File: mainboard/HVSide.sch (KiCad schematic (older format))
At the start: 36 parts, among them J10 IMD_TS-, J7 ProminentIndicator, J8 HV, J9 IMD_TS+, Q15 BULB49D, Q16 TSM2312, U13 ISOW7841, U14 LTC1865L, U15 LTC6259, U16 REF3433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

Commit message: change isoadc in schematic and documents
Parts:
- removed unit 2 of U13
- removed U14: LTC1865L, Package_SO:SSOP-10_3.9x4.9mm_P1.00mm, symbol MainBoard:LTC1865L
- added C13: 10n, symbol Device:C_Small
- added R52, R53: 22, symbol Device:R
- added R54: 2k, symbol Device:R_Small
- added R55: 680, symbol Device:R_Small
- added R56: 100k, symbol Device:R_Small
- added U14: Si8900, symbol si8900:Si8900
- added U20: TCMT1103, Package_SO:SOP-4_4.4x2.6mm_P1.27mm, symbol Isolator:TCMT1103
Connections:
- net labels added: ISOADC_RX, ISOADC_TX, RST_ADCB, ~RST~_ADCA
- net labels removed: CS, MISO, MOSI, SCK
- wire segments 135 -> 146
- no-connect marks 0 -> 6
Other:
- note removed: "UPDATE COMPONENT TO 10 PIN PACKAGE"

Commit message: i2c isoadc 8901
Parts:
- removed U14: Si8900, symbol si8900:Si8900
- added R?: 5k, symbol Device:R
- added U?: Si8901, symbol si8900:Si8901
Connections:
- net +3V3: now also U?.10 (VDDB), U?.16 (VDDB)
- net -BATT: now also U?.8 (GNDA)
- net 3V3ISO: now also R?.2, U?.1 (VDDA)
- net GND: now also U?.9 (GNDB)
- net PackV: now also U?.4 (AIN1)
- net TSV: now also U?.3 (AIN0)
- net ~RST~_ADCA: now also U?.6 (~RST~)
- net at R53.2: now also U?.12 (SDA)
- net at R52.2: now also U?.13 (SCL)
- net ISOADC_RX renamed SCL
- net ISOADC_TX renamed SDA
- new net: R?.1, U?.7 (RSDA)
- no-connect marks 6 -> 5
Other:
- moved on the sheet: R52, R53
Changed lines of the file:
@@
 Wire Notes Line
 	3450 750  3450 1900
-NoConn ~ 4750 1250
-NoConn ~ 4750 1150
+NoConn ~ 5100 1250
+NoConn ~ 5100 1150
 $Comp
 L Device:R R53
 U 1 1 6041ED95
-P 4950 1450
-F 0 "R53" V 4950 1450 50  0000 C CNN
-F 1 "22" V 5050 1450 50  0000 C CNN
-F 2 "" V 4880 1450 50  0001 C CNN
-F 3 "~" H 4950 1450 50  0001 C CNN
-	1    4950 1450
+P 5300 1450
+F 0 "R53" V 5400 1450 50  0000 C CNN
+F 1 "22" V 5300 1450 50  0000 C CNN
+F 2 "" V 5230 1450 50  0001 C CNN
+F 3 "~" H 5300 1450 50  0001 C CNN
+	1    5300 1450
 	0    1    1    0
 $EndComp
@@
 L Device:R R52
 U 1 1 6041E63C
-P 4950 1350
-F 0 "R52" V 4950 1350 50  0000 C CNN
-F 1 "22" V 4850 1350 50  0000 C CNN
-F 2 "" V 4880 1350 50  0001 C CNN
-F 3 "~" H 4950 1350 50  0001 C CNN
-	1    4950 1350
-	0    1    1    0
-$EndComp
-NoConn ~ 3950 1150
-Wire Wire Line
-	3950 1250 3650 1250
-Text Label 3650 1250 0    50   ~ 0
+P 5300 1350
+F 0 "R52" V 5200 1350 50  0000 C CNN
+F 1 "22" V 5300 1350 50  0000 C CNN
+F 2 "" V 5230 1350 50  0001 C CNN
+F 3 "~" H 5300 1350 50  0001 C CNN
+	1    5300 1350
+	0    1    1    0
+$EndComp
+NoConn ~ 4300 1150
+Text Label 4000 1250 0    50   ~ 0
 TSV
-Wire Wire Line
-	3950 1350 3650 1350
-Text Label 3650 1350 0    50   ~ 0
+Text Label 4000 1350 0    50   ~ 0
 PackV
-NoConn ~ 3950 1450
-NoConn ~ 3950 1550
+NoConn ~ 4300 1450
 $Comp
 L power:-BATT #PWR0100
 U 1 1 5B56F926
-P 3850 1750
-F 0 "#PWR0100" H 3850 1600 50  0001 C CNN
-F 1 "-BATT" V 3850 1900 50  0000 L CNN
-F 2 "" H 3850 1750 50  0001 C CNN
-F 3 "" H 3850 1750 50  0001 C CNN
-	1    3850 1750
+P 4200 1750
+F 0 "#PWR0100" H 4200 1600 50  0001 C CNN
+F 1 "-BATT" V 4200 1900 50  0000 L CNN
+F 2 "" H 4200 1750 50  0001 C CNN
+F 3 "" H 4200 1750 50  0001 C CNN
+	1    4200 1750
 	0    -1   -1   0
 $EndComp
-Wire Wire Line
-	3950 1750 3850 1750
-$Comp
-L si8900:Si8900 U14
-U 1 1 603C04CE
-P 4350 1350
-F 0 "U14" H 4350 1875 50  0000 C CNN
-F 1 "Si8900" H 4350 1784 50  0000 C CNN
-F 2 "" H 4200 1800 50  0001 C CNN
-F 3 "" H 4200 1800 50  0001 C CNN
-	1    4350 1350
-	1    0    0    -1
-$EndComp
-Wire Wire Line
-	3650 1050 3950 1050
-Text Label 3650 1050 0    50   ~ 0
+Text Label 4000 1050 0    50   ~ 0
 3V3ISO
 Text Notes 3450 750  0    50   ~ 0
 ISOLATED PACK VOLTAGE ADC WITH SPI ISOLATOR
-NoConn ~ 4750 1550
+NoConn ~ 5100 1550
 $Comp
 L power:+3V3 #PWR015
 U 1 1 6046C081
-P 4750 1050
-F 0 "#PWR015" H 4750 900 50  0001 C CNN
-F 1 "+3V3" V 4750 1200 50  0000 L CNN
-F 2 "" H 4750 1050 50  0001 C CNN
-F 3 "" H 4750 1050 50  0001 C CNN
-	1    4750 1050
+P 5100 1050
+F 0 "#PWR015" H 5100 900 50  0001 C CNN
+F 1 "+3V3" V 5100 1200 50  0000 L CNN
+F 2 "" H 5100 1050 50  0001 C CNN
+F 3 "" H 5100 1050 50  0001 C CNN
+	1    5100 1050
 	0    1    1    0
 $EndComp
@@
 L power:+3V3 #PWR099
 U 1 1 6046CB1E
-P 4750 1650
-F 0 "#PWR099" H 4750 1500 50  0001 C CNN
-F 1 "+3V3" V 4750 1800 50  0000 L CNN
-F 2 "" H 4750 1650 50  0001 C CNN
-F 3 "" H 4750 1650 50  0001 C CNN
-	1    4750 1650
+P 5100 1650
+F 0 "#PWR099" H 5100 1500 50  0001 C CNN
+F 1 "+3V3" V 5100 1800 50  0000 L CNN
+F 2 "" H 5100 1650 50  0001 C CNN
+F 3 "" H 5100 1650 50  0001 C CNN
+	1    5100 1650
 	0    1    1    0
 $EndComp
@@
 L power:GND #PWR0143
 U 1 1 6046D345
-P 4750 1750
-F 0 "#PWR0143" H 4750 1500 50  0001 C CNN
-F 1 "GND" V 4750 1600 50  0000 R CNN
-F 2 "" H 4750 1750 50  0001 C CNN
-F 3 "" H 4750 1750 50  0001 C CNN
-	1    4750 1750
+P 5100 1750
+F 0 "#PWR0143" H 5100 1500 50  0001 C CNN
+F 1 "GND" V 5100 1600 50  0000 R CNN
+F 2 "" H 5100 1750 50  0001 C CNN
+F 3 "" H 5100 1750 50  0001 C CNN
+	1    5100 1750
 	0    -1   -1   0
 $EndComp
 Wire Wire Line
-	4800 1350 4750 1350
-Wire Wire Line
-	4750 1450 4800 1450
-Wire Wire Line
-	5100 1350 5150 1350
-Wire Wire Line
-	5150 1450 5100 1450
-Text HLabel 5150 1450 2    50   Input ~ 0
-ISOADC_TX
-Text HLabel 5150 1350 2    50   Input ~ 0
-ISOADC_RX
-Text Label 3550 1650 0    50   ~ 0
+	5150 1350 5100 1350
+Wire Wire Line
+	5100 1450 5150 1450
+Wire Wire Line
+	5450 1350 5500 1350
+Wire Wire Line
+	5500 1450 5450 1450
+Text HLabel 5500 1450 2    50   Input ~ 0
+SDA
+Text HLabel 5500 1350 2    50   Input ~ 0
+SCL
+Text Label 3900 1550 0    50   ~ 0
 ~RST~_ADCA
-Wire Wire Line
-	3550 1650 3950 1650
 Text Label 5650 1150 0    50   ~ 0
 ~RST~_ADCA
@@
 $EndComp
 Wire Notes Line
-	4250 1850 4300 1850
-Wire Notes Line
-	4300 1850 4300 1000
-Wire Notes Line
-	4400 1850 4350 1850
-Wire Notes Line
-	4350 1850 4350 1000
+	4600 1850 4650 1850
+Wire Notes Line
+	4650 1850 4650 1000
+Wire Notes Line
+	4800 1850 4750 1850
+Wire Notes Line
+	4750 1850 4750 1000
 Wire Notes Line
 	6400 1750 6400 1350
@@
 Wire Wire Line
 	6050 1150 6050 1450
+Wire Wire Line
+	4300 1750 4200 1750
+Wire Wire Line
+	4300 1350 4000 1350
+Wire Wire Line
+	4300 1250 4000 1250
+$Comp
+L si8900:Si8901 U?
+U 1 1 603E5D4E
+P 4700 1350
+F 0 "U?" H 4700 1875 50  0000 C CNN
+F 1 "Si8901" H 4700 1784 50  0000 C CNN
+F 2 "" H 4550 1800 50  0001 C CNN
+F 3 "" H 4550 1800 50  0001 C CNN
+	1    4700 1350
+	1    0    0    -1
+$EndComp
+$Comp
+L Device:R R?
+U 1 1 603F9D47
+P 3800 1250
+F 0 "R?" V 3900 1250 50  0000 C CNN
+F 1 "5k" V 3800 1250 50  0000 C CNN
+F 2 "" V 3730 1250 50  0001 C CNN
+F 3 "~" H 3800 1250 50  0001 C CNN
+	1    3800 1250
+	-1   0    0    1
+$EndComp
+Wire Wire Line
+	3900 1550 4300 1550
+Wire Wire Line
+	3800 1650 3800 1400
+Wire Wire Line
+	3800 1050 3800 1100
+Wire Wire Line
+	3800 1650 4300 1650
+Wire Wire Line
+	3800 1050 4300 1050
 $EndSCHEMATC

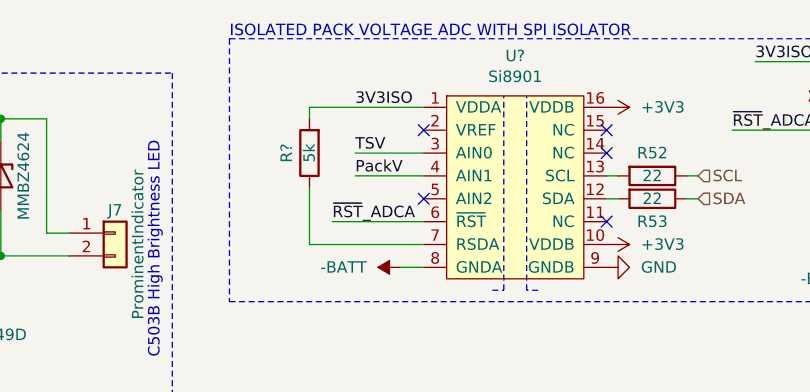
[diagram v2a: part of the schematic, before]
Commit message: adding handcart detection
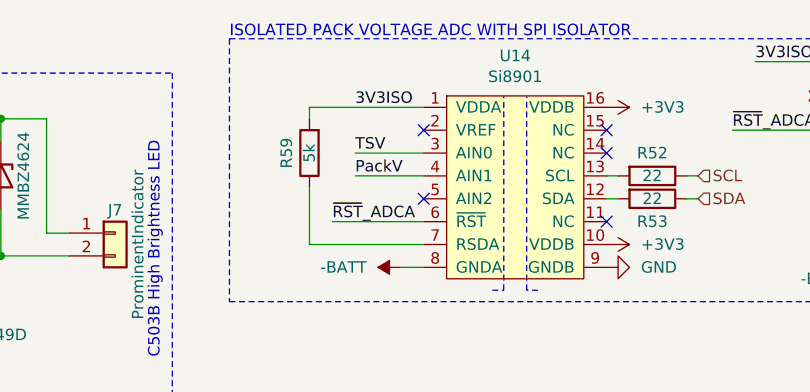
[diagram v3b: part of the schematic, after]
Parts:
- gave numbers to parts that had none: 2
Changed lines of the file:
@@
 	4300 1250 4000 1250
 $Comp
-L si8900:Si8901 U?
+L si8900:Si8901 U14
 U 1 1 603E5D4E
 P 4700 1350
-F 0 "U?" H 4700 1875 50  0000 C CNN
+F 0 "U14" H 4700 1875 50  0000 C CNN
 F 1 "Si8901" H 4700 1784 50  0000 C CNN
 F 2 "" H 4550 1800 50  0001 C CNN
@@
 $EndComp
 $Comp
-L Device:R R?
+L Device:R R59
 U 1 1 603F9D47
 P 3800 1250
-F 0 "R?" V 3900 1250 50  0000 C CNN
+F 0 "R59" V 3900 1250 50  0000 C CNN
 F 1 "5k" V 3800 1250 50  0000 C CNN
 F 2 "" V 3730 1250 50  0001 C CNN

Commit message: Shutdown logic to use gates, changed mosfets
Shutdown ported from new car, mosfets changed to higher VGS max
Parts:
- removed C27: 1u, Capacitor_SMD:C_0805_2012Metric, symbol Device:C
- removed U13: ISOW7841, MainBoard:SOIC-16, symbol MainBoard:ISOW7841
- removed U16: REF3433, MainBoard:SOT-23-6, symbol MainBoard:REF3433
- added C31, C32: 10u, symbol Device:C
- added U22: LM1117-3.3, symbol Regulator_Linear:LM1117-3.3
- added U23: RFMM-0505S, symbol MainBoard:RFMM-0505S
- D5: value BZD27C56P -> BZD27C56P 56V
- D6, D7: value MMBZ4624 -> MMBZ4624 4V7
- Q16: value TSM2312 -> NTR4003
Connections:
- net +5V: now also C31.1, U23.1 (Vin+)
- net -BATT: now also C32.2, U22.1 (GND), U23.5 (Vout-)
- net 3V3ISO: now also R59.1, C32.1, U22.2 (VO); no longer R59.2
- net 5VISO: now also U22.3 (VI), U23.7 (Vout+)
- net GND: now also C31.2, U23.2 (Vin-)
- net at U14.7 (RSDA): now also R59.2; no longer R59.1
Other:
- note added: "25mA max"
- note added: "4.7V in the connector \nwhen V_TS>60V"
- note added: "CHECK: unpopulated"
- note added: "ISOLATED 3.3V VOLTAGE SOURCE"
- note added: "Isolated DCDC"
- note added: "Limited at 4.7V by D7\nC503B High Brightness LED"
- note added: "Open drain outputs"
- note added: "Over and under voltage monitoring"
- note added: "V_TS max is 600V"
- note removed: "C503B High Brightness LED"
- note removed: "ISOLATED 3.3V VOLTAGE REFERENCE"
- moved on the sheet: C28, R59, U17

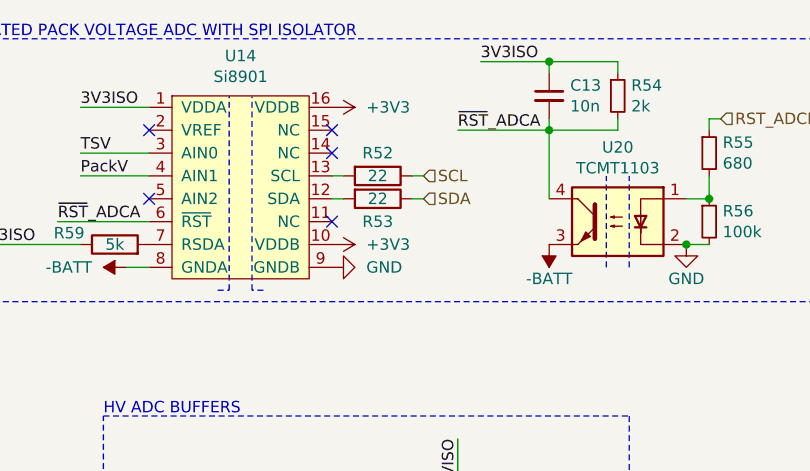
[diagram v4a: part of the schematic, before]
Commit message: removed erroneus R on I2c
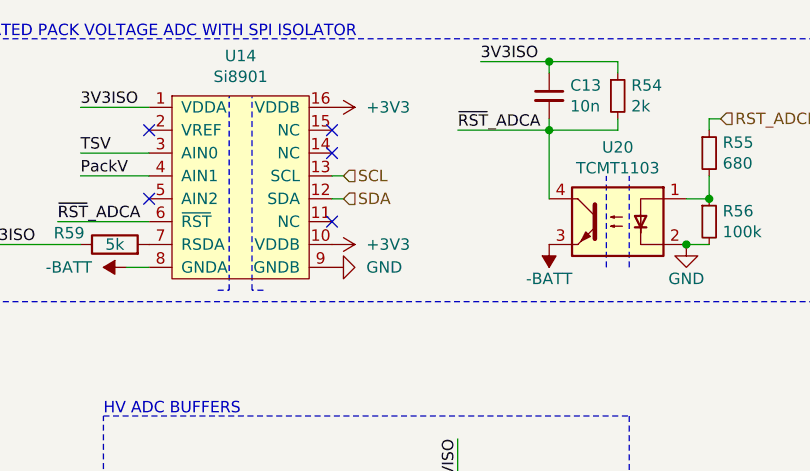
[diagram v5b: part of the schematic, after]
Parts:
- removed R52, R53: 22, symbol Device:R
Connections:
- net SCL: now also U14.13 (SCL)
- net SDA: now also U14.12 (SDA)
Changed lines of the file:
@@
 NoConn ~ 5100 1250
 NoConn ~ 5100 1150
-$Comp
-L Device:R R53
-U 1 1 6041ED95
-P 5300 1450
-F 0 "R53" V 5400 1450 50  0000 C CNN
-F 1 "22" V 5300 1450 50  0000 C CNN
-F 2 "" V 5230 1450 50  0001 C CNN
-F 3 "~" H 5300 1450 50  0001 C CNN
-	1    5300 1450
-	0    1    1    0
-$EndComp
-$Comp
-L Device:R R52
-U 1 1 6041E63C
-P 5300 1350
-F 0 "R52" V 5200 1350 50  0000 C CNN
-F 1 "22" V 5300 1350 50  0000 C CNN
-F 2 "" V 5230 1350 50  0001 C CNN
-F 3 "~" H 5300 1350 50  0001 C CNN
-	1    5300 1350
-	0    1    1    0
-$EndComp
 NoConn ~ 4300 1150
 Text Label 4000 1250 0    50   ~ 0
@@
 $EndComp
 Wire Wire Line
-	5150 1350 5100 1350
+	5100 1350 5150 1350
 Wire Wire Line
-	5100 1450 5150 1450
-Wire Wire Line
-	5450 1350 5500 1350
-Wire Wire Line
-	5500 1450 5450 1450
-Text HLabel 5500 1450 2    50   Input ~ 0
+	5150 1450 5100 1450
+Text HLabel 5150 1450 2    50   Input ~ 0
 SDA
-Text HLabel 5500 1350 2    50   Input ~ 0
+Text HLabel 5150 1350 2    50   Input ~ 0
 SCL
 Text Label 3900 1550 0    50   ~ 0

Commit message: ported prominent of newcar as optional
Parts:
- added C? (x2): 1uF, symbol Device:C
- added J?: PROMINENT, Connector_Molex:Molex_Micro-Fit_3.0_43045-0412_2x02_P3.00mm_Vertical, symbol Connector_Generic:Conn_02x02_Odd_Even
- added R?: 1k, Resistor_SMD:R_0805_2012Metric, symbol Device:R
- added R?: 10M, Resistor_SMD:R_1210_3225Metric, symbol Device:R
- added R?: 100k, Resistor_SMD:R_0805_2012Metric, symbol Device:R
- added U?: ROE-0505S, symbol MainBoard:ROE-0505S
- added U?: ADCMP350, Package_TO_SOT_SMD:Analog_KS-4, symbol Comparator:ADCMP350
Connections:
- net +TS: now also R?.2
- net -BATT: now also C?.2, R?.2, U?.2 (GND), U?.5 (Vout-)
- new net: R?.1, R?.1, U?.1 (VIN)
- new net 1st_CELL_5V: C?.1, J?.1 (Pin_1), U?.1 (Vin+)
- new net 1st_CELL_GND: C?.2, J?.3 (Pin_3), U?.2 (Vin-)
- new net PROMINENT+: J?.2 (Pin_2), R?.1
- new net PROMINENT-: J?.4 (Pin_4), U?.3
- new net PROM_5V: C?.1, R?.2, U?.4 (VCC), U?.7 (Vout+)
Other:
- note added: "PROMINENT INDICATOR"
- note added: "old PROMINENT INDICATOR CURRENT SOURCE"
- note removed: "PROMINENT INDICATOR CURRENT SOURCE"
- moved on the sheet: D5, D6, D7, F1, J10, J7, J8, J9, Q15, R36, R37, R38
